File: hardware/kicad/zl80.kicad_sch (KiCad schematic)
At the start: 112 parts, among them J1 12 V DC in, J2 SCART, J3 RGB board (later), J4 Joystick 1 (Atari / Sega), J5 Joystick 2 (Atari / Sega), J6 PS/2 keyboard, J7 ISP for the ATmega, J8 Expansion (8255 PA, PC4-7), J9 USB serial (FTDI cable, 5 V), Q1 2N4401 video buffer, SW1 Reset, U1 Z84C0004 (Z80 CMOS), U10 74HCT04, U11 74HCT74 paging on / AY clock, U12 74HCT02 AY bus control, U13 DS1813-5 reset, U14 R-78E5.0-1.0 (or 7805), U15 TMS9918A, U16 62256 VRAM (16 KB used), U17 74HCT574 VRAM row latch, U18 AY-3-8910, U19 74HCT157 joystick directions, U2 SST39SF040 flash, pages 0-31, U20 74HCT157 joystick buttons, U21 82C55A, U22 ATmega328P: PS/2 to key matrix, U23 MC68B50 ACIA, U24 74HCT574 VRAM column latch, U25 74HCT574 VRAM write data, U26 74HCT04 VRAM strobes, U3 AS6C4008 SRAM, pages 32-63, U4 74HCT670 page bits 0-3, U5 74HCT670 page bits 4-5, U6 74HCT138 I/O 80h-BFh, U7 74HCT138 I/O 00h-7Fh, U8 74HCT32, U9 74HCT32, X1 7.3728 MHz oscillator, Y1 10.738635 MHz

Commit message: Replace the 6850 with a UM245R USB FIFO module
The board talks to the PC through FTDI's UM245R module (FT245R on a
24-pin DIP footprint) instead of an MC68B50 with a 7.3728 MHz
oscillator and an FTDI cable. The PC still sees a serial port, so
Send to board and the HEX loader protocol are unchanged.

- Port 80h: USB data. Port 81h: status (read only), RXF# on D0 and
  TXE# on D1 through a 74HCT125.
- Strobes from a new 74HCT32 plus a spare 74HCT02 and 74HCT04 gate:
  RD# = USBSEL|/RD|A0, WR = NOR(USBSEL|/WR, A0), status = USBSEL|/RD|/A0.
- Self-powered wiring from the UM245R datasheet (FT_000202, 4.2 and
  7.2): J2 open, J1 2-3, USB 5 V to PU2, PU1 to RST#.
- Kernel: no serial set-up; GETC, PUTC and the interrupt handler read
  the status port. Emulator: a 256-byte receive FIFO that makes the
  PC wait when full, as the FT245R does; reading an empty FIFO or
  writing the status port stops the program.

Checked: KiCad 9 ERC reports 0 violations and its netlist matches
zl80-netlist.txt (192 nets). In the emulator, programs of 99 to 2969
bytes load while another runs and on a board with nothing in flash; a
whole HEX file sent without waiting for answers also loads; bad
records get !. Fantasy displays match the baseline; 15 of 17 examples
run on the board. Not tried with a real UM245R.

Co-Authored-By: Claude Opus 5.5 <noreply@anthropic.com>
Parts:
- removed J9: USB serial (FTDI cable, 5 V), Connector_PinHeader_2.54mm:PinHeader_1x06_P2.54mm_Vertical, symbol zl80:Serial_FTDI6
- removed X1: 7.3728 MHz oscillator, Oscillator:Oscillator_DIP-14, symbol zl80:Oscillator_DIP14
- added C35: 100n, Capacitor_THT:C_Disc_D5.0mm_W2.5mm_P5.00mm, symbol zl80:C
- added U27: 74HCT32 USB FIFO strobes, Package_DIP:DIP-14_W7.62mm, symbol zl80:74HCT32
- added U28: 74HCT125 USB status on D0, D1, Package_DIP:DIP-14_W7.62mm, symbol zl80:74HCT125
- U23: value MC68B50 ACIA -> UM245R USB FIFO module; symbol zl80:MC68B50 -> zl80:UM245R
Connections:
- net SER_RTS is gone; now on net D1: U23.5 (DB1)
- net SER_RX is gone; now on net D4: U23.2 (DB4)
- net SER_TX is gone; now on net D7: U23.6 (DB7)
- net +5V: now also U23.15 (VCC), U23.21 (VCC), C35.1, U27.14 (VCC), U28.10 (~{3OE}), U28.13 (~{4OE}), U28.14 (VCC); no longer U23.10 (CS1), U23.12 (VCC), U23.8 (CS0)
- net A0: now also U10.13 (6A), U12.9 (3B), U27.5 (2B); no longer U23.11 (RS)
- net D0: now also U23.1 (DB0), U28.3 (1Y); no longer U23.22 (D0)
- net D1: now also U28.6 (2Y); no longer U23.21 (D1)
- net D2: now also U23.3 (DB2); no longer U23.20 (D2)
- net D3: now also U23.10 (DB3); no longer U23.19 (D3)
- net D4: no longer U23.18 (D4)
- net D5: now also U23.8 (DB5); no longer U23.17 (D5)
- net D6: now also U23.9 (DB6); no longer U23.16 (D6)
- net D7: no longer U23.15 (D7)
- net GND: now also U23.7 (GND), C35.2, U27.7 (GND), U28.12 (4A), U28.7 (GND), U28.9 (3A); no longer U12.8 (3A), U12.9 (3B), U23.1 (VSS), U23.23 (~{DCD})
- net ~{IORQ}: no longer U10.13 (6A)
- net ~{RD}: now also U27.2 (1B)
- net ~{WR}: now also U27.13 (4B); no longer U23.13 (R/~{W})
- net USBWR: now reaches U12.10 (3Y)
- net USBWR: now also U23.18 (WR)
- net ACLK: no longer names the net of U23.4 (VIO)
- net ACLK: no longer U23.3 (RXCLK)
- net E_ACIA renamed USB_VBUS
- net USB_VBUS: now also U23.16 (PU2); no longer U10.12 (6Y)
- net ~{ACIA_CS} renamed ~{USB_CS}
- net ~{USB_CS}: now also U27.1 (1A), U27.12 (4A); no longer U23.9 (~{CS2})
- new net USB_RST: U23.17 (PU1), U23.20 (RST#)
- new net USB_RXF: U23.23 (RXF#), U28.2 (1A)
- new net USB_TXE: U23.22 (TXE#), U28.5 (2A)
- new net ~{A0}: U10.12 (6Y), U27.10 (3B)
- new net ~{USBRDQ}: U27.3 (1Y=1A|1B), U27.4 (2A), U27.9 (3A)
- new net ~{USBRD}: U23.12 (RD#), U27.6 (2Y=1A|1B)
- new net ~{USBST}: U27.8 (3Y=1A|1B), U28.1 (~{1OE}), U28.4 (~{2OE})
- new net ~{USBWRQ}: U12.8 (3A), U27.11 (4Y=1A|1B)
- no-connect marks 53 -> 54
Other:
- moved on the sheet: J1, JP1, SW1, U14, U23, Y1

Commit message: KiCad schematic: split into pages
The schematic is now a root sheet with one box per page and five
pages: CPU, memory and decoding; video; sound and joysticks; keyboard
and USB; power, reset and TV. Signals that go to another page use
global labels, the rest plain labels. Each chip's 100 nF capacitor
is on the chip's page and names it in its value.

sch.py gains a Project with pages; check_schematic.py follows the
sub-sheets from the root. The circuit is unchanged: KiCad 9 ERC
reports 0 violations, and the netlist KiCad exports still matches
zl80-netlist.txt (192 nets). One 100 nF capacitor fewer: the ISP
header no longer counts as a chip.

Co-Authored-By: Claude Opus 5.5 <noreply@anthropic.com>
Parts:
- removed C1, C2: 10u, Capacitor_THT:CP_Radial_D6.3mm_P2.50mm, symbol zl80:C_Polarized
- removed C10, C11, C12, C13, C14, C15, C16, C17, C18, C19, C20, C21, C22, C23, C24, C25, C26, C27, C28, C29, C32, C33, C34, C35, C5, C6, C7, C8, C9: 100n, Capacitor_THT:C_Disc_D5.0mm_W2.5mm_P5.00mm, symbol zl80:C
- removed C3, C4: 100u, Capacitor_THT:CP_Radial_D6.3mm_P2.50mm, symbol zl80:C_Polarized
- removed C30, C31: 22p, Capacitor_THT:C_Disc_D5.0mm_W2.5mm_P5.00mm, symbol zl80:C
- removed D1: 1N5819, Diode_THT:D_DO-41_SOD81_P10.16mm_Horizontal, symbol zl80:D
- removed D2: Power, LED_THT:LED_D3.0mm, symbol zl80:LED
- removed D3: BAT85, Diode_THT:D_DO-41_SOD81_P10.16mm_Horizontal, symbol zl80:D
- removed FB1: Ferrite bead, Inductor_THT:L_Axial_L5.3mm_D2.2mm_P7.62mm_Horizontal_Vishay_IM-1, symbol zl80:Ferrite_Bead
- removed J1: 12 V DC in, Connector_BarrelJack:BarrelJack_Horizontal, symbol zl80:Barrel_Jack
- removed J2: SCART, symbol zl80:SCART
- removed J3: RGB board (later), Connector_PinHeader_2.54mm:PinHeader_1x07_P2.54mm_Vertical, symbol zl80:RGB_Header
- removed J4: Joystick 1 (Atari / Sega), symbol zl80:DB9_Joystick
- removed J5: Joystick 2 (Atari / Sega), symbol zl80:DB9_Joystick
- removed J6: PS/2 keyboard, symbol zl80:MiniDIN6_PS2
- removed J7: ISP for the ATmega, Connector_PinHeader_2.54mm:PinHeader_2x03_P2.54mm_Vertical, symbol zl80:AVR_ISP6
- removed J8: Expansion (8255 PA, PC4-7), Connector_PinHeader_2.54mm:PinHeader_2x07_P2.54mm_Vertical, symbol zl80:Expansion_2x7
- removed JP1: Flash write enable, Connector_PinHeader_2.54mm:PinHeader_1x02_P2.54mm_Vertical, symbol zl80:Jumper_2
- removed Q1: 2N4401 video buffer, Package_TO_SOT_THT:TO-92_Inline, symbol zl80:NPN_BCE
- removed R1, R10, R11, R12, R15, R2, R3, R4, R5, R6, R7, R8, R9: 10k, Resistor_THT:R_Axial_DIN0207_L6.3mm_D2.5mm_P10.16mm_Horizontal, symbol zl80:R
- removed R13, R14: 4.7k, Resistor_THT:R_Axial_DIN0207_L6.3mm_D2.5mm_P10.16mm_Horizontal, symbol zl80:R
- removed R16, R17, R18: 3k, Resistor_THT:R_Axial_DIN0207_L6.3mm_D2.5mm_P10.16mm_Horizontal, symbol zl80:R
- removed R19, R22, R29, R30, R31, R32: 1k, Resistor_THT:R_Axial_DIN0207_L6.3mm_D2.5mm_P10.16mm_Horizontal, symbol zl80:R
- removed R20, R21: 2.2k, Resistor_THT:R_Axial_DIN0207_L6.3mm_D2.5mm_P10.16mm_Horizontal, symbol zl80:R
- removed R23, R24: 47k, Resistor_THT:R_Axial_DIN0207_L6.3mm_D2.5mm_P10.16mm_Horizontal, symbol zl80:R
- removed R25: 130, Resistor_THT:R_Axial_DIN0207_L6.3mm_D2.5mm_P10.16mm_Horizontal, symbol zl80:R
- removed R26: 470, Resistor_THT:R_Axial_DIN0207_L6.3mm_D2.5mm_P10.16mm_Horizontal, symbol zl80:R
- removed R27, R28: 75, Resistor_THT:R_Axial_DIN0207_L6.3mm_D2.5mm_P10.16mm_Horizontal, symbol zl80:R
- removed RN1, RN2: 10k x 8, Resistor_THT:R_Array_SIP9, symbol zl80:R_Network08
- removed SW1: Reset, Button_Switch_THT:SW_PUSH_6mm, symbol zl80:SW_Push
- removed U1: Z84C0004 (Z80 CMOS), Package_DIP:DIP-40_W15.24mm, symbol zl80:Z80_CPU
- removed U10: 74HCT04, Package_DIP:DIP-14_W7.62mm, symbol zl80:74HCT04
- removed U11: 74HCT74 paging on / AY clock, Package_DIP:DIP-14_W7.62mm, symbol zl80:74HCT74
- removed U12: 74HCT02 AY bus control, Package_DIP:DIP-14_W7.62mm, symbol zl80:74HCT02
- removed U13: DS1813-5 reset, Package_TO_SOT_THT:TO-92_Inline, symbol zl80:DS1813
- removed U14: R-78E5.0-1.0 (or 7805), Package_TO_SOT_THT:TO-220-3_Vertical, symbol zl80:Regulator_5V
- removed U15: TMS9918A, Package_DIP:DIP-40_W15.24mm, symbol zl80:TMS9918A
- removed U16: 62256 VRAM (16 KB used), Package_DIP:DIP-28_W15.24mm, symbol zl80:62256
- removed U17: 74HCT574 VRAM row latch, Package_DIP:DIP-20_W7.62mm, symbol zl80:74HCT574
- removed U18: AY-3-8910, Package_DIP:DIP-40_W15.24mm, symbol zl80:AY-3-8910
- removed U19: 74HCT157 joystick directions, Package_DIP:DIP-16_W7.62mm, symbol zl80:74HCT157
- removed U2: SST39SF040 flash, pages 0-31, Package_DIP:DIP-32_W15.24mm, symbol zl80:SST39SF040
- removed U20: 74HCT157 joystick buttons, Package_DIP:DIP-16_W7.62mm, symbol zl80:74HCT157
- removed U21: 82C55A, Package_DIP:DIP-40_W15.24mm, symbol zl80:82C55A
- removed U22: ATmega328P: PS/2 to key matrix, Package_DIP:DIP-28_W7.62mm, symbol zl80:ATmega328P
- removed U23: UM245R USB FIFO module, Package_DIP:DIP-24_W15.24mm, symbol zl80:UM245R
- removed U24: 74HCT574 VRAM column latch, Package_DIP:DIP-20_W7.62mm, symbol zl80:74HCT574
- removed U25: 74HCT574 VRAM write data, Package_DIP:DIP-20_W7.62mm, symbol zl80:74HCT574
- removed U26: 74HCT04 VRAM strobes, Package_DIP:DIP-14_W7.62mm, symbol zl80:74HCT04
- removed U27: 74HCT32 USB FIFO strobes, Package_DIP:DIP-14_W7.62mm, symbol zl80:74HCT32
- removed U28: 74HCT125 USB status on D0, D1, Package_DIP:DIP-14_W7.62mm, symbol zl80:74HCT125
- removed U3: AS6C4008 SRAM, pages 32-63, Package_DIP:DIP-32_W15.24mm, symbol zl80:AS6C4008
- removed U4: 74HCT670 page bits 0-3, Package_DIP:DIP-16_W7.62mm, symbol zl80:74HCT670
- removed U5: 74HCT670 page bits 4-5, Package_DIP:DIP-16_W7.62mm, symbol zl80:74HCT670
- removed U6: 74HCT138 I/O 80h-BFh, Package_DIP:DIP-16_W7.62mm, symbol zl80:74HCT138
- removed U7: 74HCT138 I/O 00h-7Fh, Package_DIP:DIP-16_W7.62mm, symbol zl80:74HCT138
- removed U8, U9: 74HCT32, Package_DIP:DIP-14_W7.62mm, symbol zl80:74HCT32
- removed Y1: 10.738635 MHz, Crystal:Crystal_HC49-4H_Vertical, symbol zl80:Crystal
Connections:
- no-connect marks 54 -> 0
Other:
- added sheet CPU, memory and decoding (cpu_memory.kicad_sch)
- added sheet Keyboard and USB (keyboard_usb.kicad_sch)
- added sheet Power, reset and TV (power_tv.kicad_sch)
- added sheet Sound and joysticks (sound.kicad_sch)
- added sheet Video: TMS9918A and VRAM (video.kicad_sch)
- note added: "ZL-80 board, generated by hardware/kicad/gen_schematic.py from docs/hardware.md. Each box is a page. Labels with the same name are connected; the labels in a frame (global labels) go to other pages. NOT BUILT OR TESTED. Check every pin against the datasheets before ordering a board."
- note removed: "ZL-80 board, generated by hardware/kicad/gen_schematic.py from docs/hardware.md. Connections are by net name. NOT BUILT OR TESTED. Check every pin against the datasheets before ordering a board."

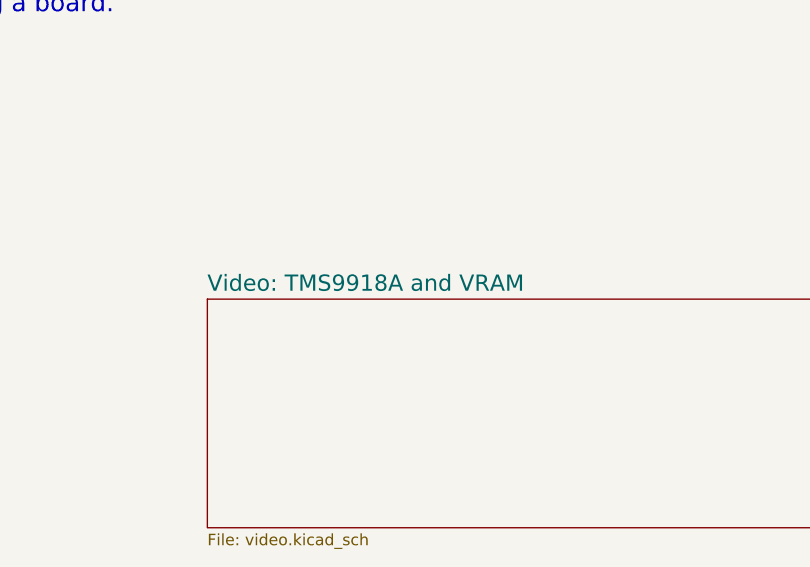
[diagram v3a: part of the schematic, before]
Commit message: Add schematic, PCB and 3D pictures to the READMEs
hardware/images holds the six schematic pages and the copper layers
as SVG (kicad-cli sch/pcb export svg) and three 3D renders as PNG
(kicad-cli pcb render: top, bottom, angled). The main README shows
the 3D views and links every schematic page and layer; the KiCad
README shows the angled view and says how to export them again.

The video page is now "Video, TMS9918A and VRAM": the colon in its
old name made an invalid Windows file name when exported. ERC and
the PCB schematic parity check are still clean.

Co-Authored-By: Claude Opus 5.5 <noreply@anthropic.com>
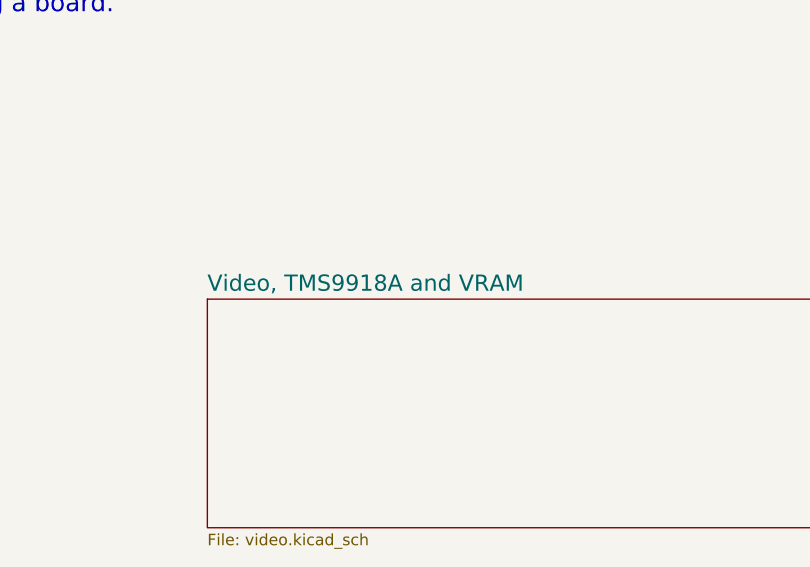
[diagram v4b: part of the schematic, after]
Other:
- sheet Video: TMS9918A and VRAM renamed Video, TMS9918A and VRAM
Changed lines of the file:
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@@
 (text "ZL-80 board, generated by hardware/kicad/gen_schematic.py from docs/hardware.md.\nEach box is a page. Labels with the same name are connected; the labels in a frame\n(global labels) go to other pages.\nNOT BUILT OR TESTED. Check every pin against the datasheets before ordering a board." (at 20 20 0) (effects (font (size 2 2)) (justify left top)))
 (sheet (at 25.4 63.5) (size 101.6 25.4) (fields_autoplaced) (stroke (width 0.1524) (type solid)) (fill (color 0 0 0 0.0000)) (property "Sheetname" "CPU, memory and decoding" (at 25.4 62.7888 0) (effects (font (size 1.8 1.8)) (justify left bottom))) (property "Sheetfile" "cpu_memory.kicad_sch" (at 25.4 89.5112 0) (effects (font (size 1.27 1.27)) (justify left top))) (instances (project "zl80" (path "/39975c11-23ed-514a-9f29-f1c34a4c379e" (page "2")))))
-(sheet (at 152.4 63.5) (size 101.6 25.4) (fields_autoplaced) (stroke (width 0.1524) (type solid)) (fill (color 0 0 0 0.0000)) (property "Sheetname" "Video: TMS9918A and VRAM" (at 152.4 62.7888 0) (effects (font (size 1.8 1.8)) (justify left bottom))) (property "Sheetfile" "video.kicad_sch" (at 152.4 89.5112 0) (effects (font (size 1.27 1.27)) (justify left top))) (instances (project "zl80" (path "/39975c11-23ed-514a-9f29-f1c34a4c379e" (page "3")))))
+(sheet (at 152.4 63.5) (size 101.6 25.4) (fields_autoplaced) (stroke (width 0.1524) (type solid)) (fill (color 0 0 0 0.0000)) (property "Sheetname" "Video, TMS9918A and VRAM" (at 152.4 62.7888 0) (effects (font (size 1.8 1.8)) (justify left bottom))) (property "Sheetfile" "video.kicad_sch" (at 152.4 89.5112 0) (effects (font (size 1.27 1.27)) (justify left top))) (instances (project "zl80" (path "/39975c11-23ed-514a-9f29-f1c34a4c379e" (page "3")))))
 (sheet (at 25.4 101.6) (size 101.6 25.4) (fields_autoplaced) (stroke (width 0.1524) (type solid)) (fill (color 0 0 0 0.0000)) (property "Sheetname" "Sound and joysticks" (at 25.4 100.8888 0) (effects (font (size 1.8 1.8)) (justify left bottom))) (property "Sheetfile" "sound.kicad_sch" (at 25.4 127.6112 0) (effects (font (size 1.27 1.27)) (justify left top))) (instances (project "zl80" (path "/39975c11-23ed-514a-9f29-f1c34a4c379e" (page "4")))))
 (sheet (at 152.4 101.6) (size 101.6 25.4) (fields_autoplaced) (stroke (width 0.1524) (type solid)) (fill (color 0 0 0 0.0000)) (property "Sheetname" "Keyboard and USB" (at 152.4 100.8888 0) (effects (font (size 1.8 1.8)) (justify left bottom))) (property "Sheetfile" "keyboard_usb.kicad_sch" (at 152.4 127.6112 0) (effects (font (size 1.27 1.27)) (justify left top))) (instances (project "zl80" (path "/39975c11-23ed-514a-9f29-f1c34a4c379e" (page "5")))))
